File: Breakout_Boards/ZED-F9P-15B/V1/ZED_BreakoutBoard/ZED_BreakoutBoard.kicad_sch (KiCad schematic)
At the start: 15 parts, among them IC1 ZED-F9P-15B, J1 142-0701-801, J2 GPS_Conn_02x04_Top_Bottom

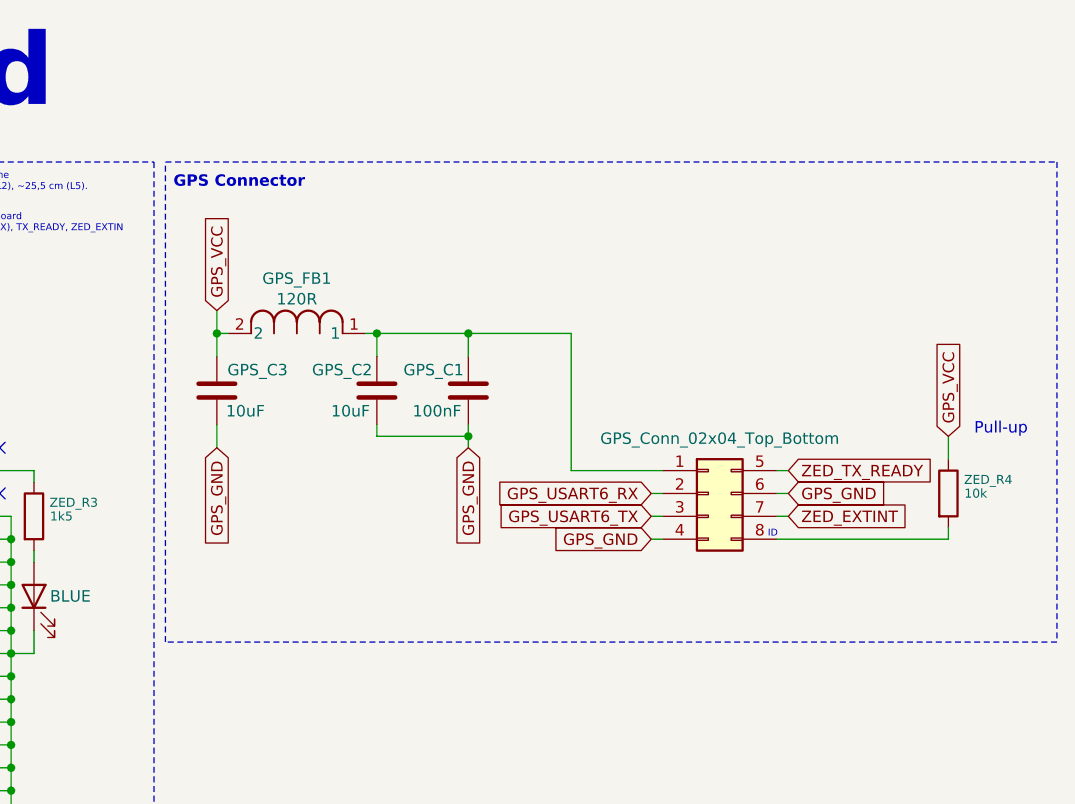
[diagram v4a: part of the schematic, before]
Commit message: fix: swipe filter breakoutboard VCC to main connector side
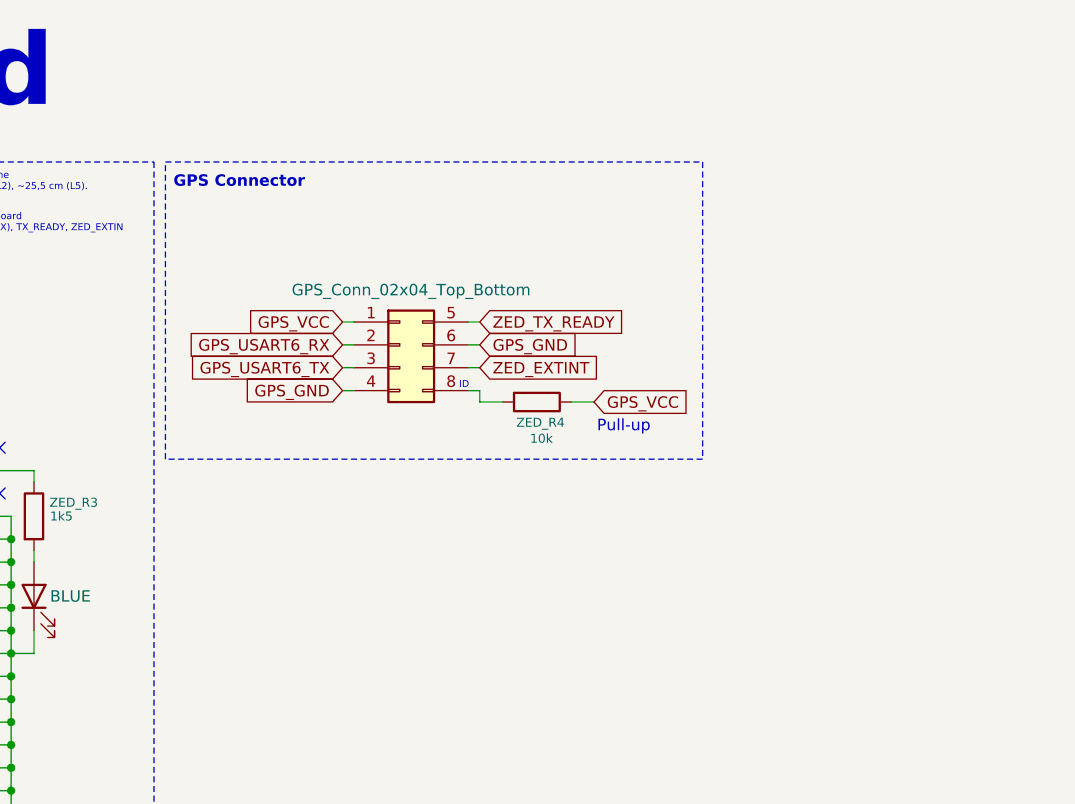
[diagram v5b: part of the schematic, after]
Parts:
- removed GPS_C1: 100nF, Capacitor_SMD:C_0603_1608Metric, symbol Device:C
- removed GPS_C2, GPS_C3: 10uF, Capacitor_SMD:C_0603_1608Metric, symbol Device:C
- removed GPS_FB1: 120R, ZED_Library:IND_25_0805_FRT, symbol ZED_Library:2508051217Y6
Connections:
- net GPS_VCC: now also J2.1 (Pin_1)
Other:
- moved on the sheet: ZED_R4

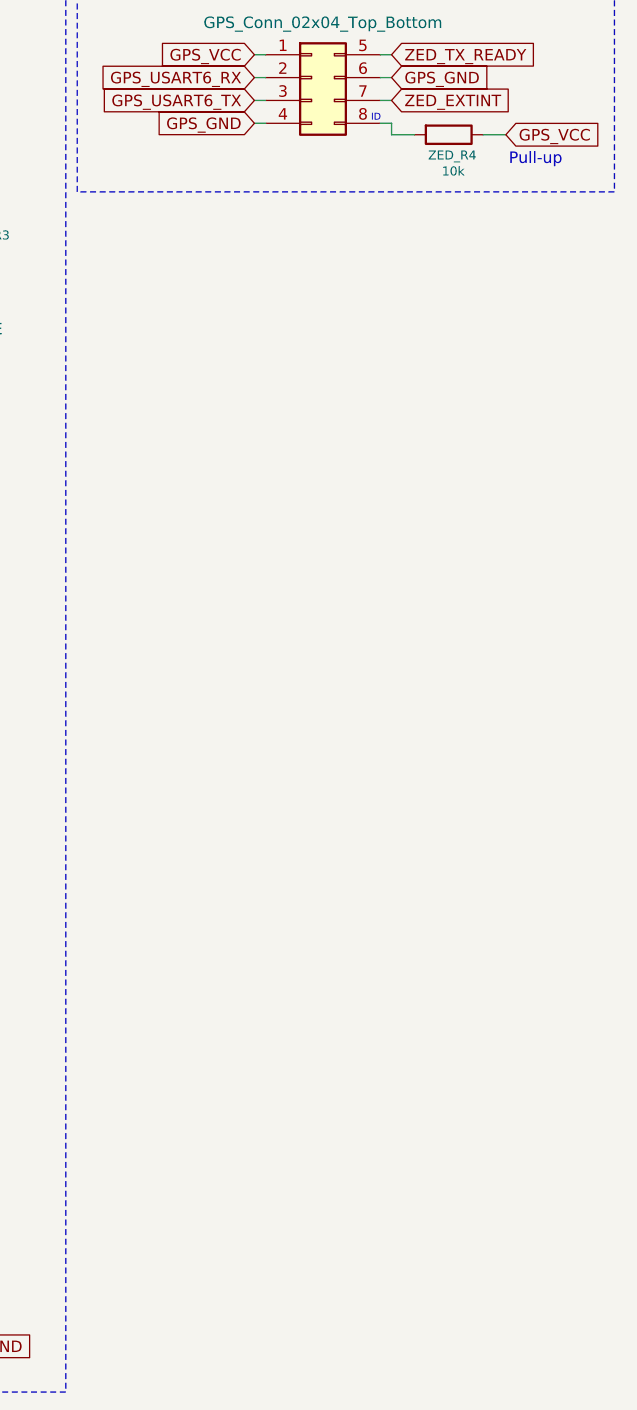
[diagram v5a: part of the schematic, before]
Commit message: feat: add mounting holes M2 & cleanup unnecessary components & add sma footprint
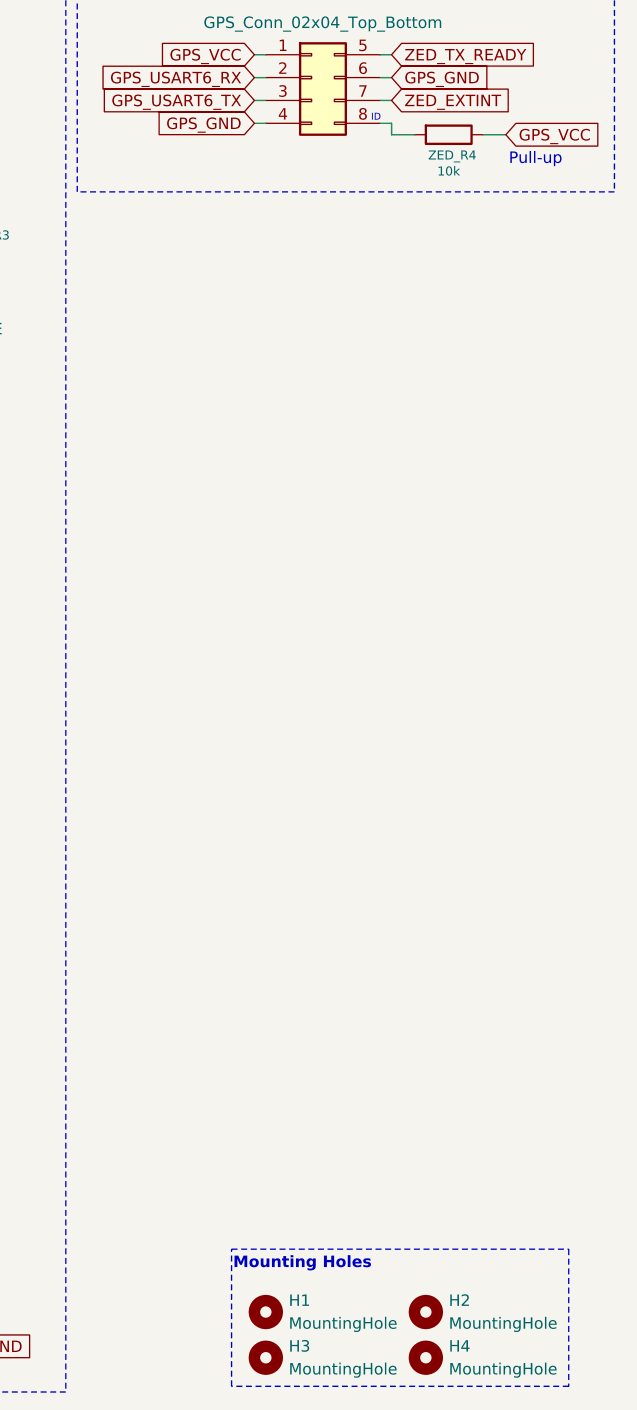
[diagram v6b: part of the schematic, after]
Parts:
- added H1, H2, H3, H4: MountingHole, MountingHole:MountingHole_2.2mm_M2, symbol Mechanical:MountingHole
- J1: footprint CONN_142-0701-801 -> ZED_Library:CONN_142-0701-801
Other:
- note added: "Mounting Holes"

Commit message: WIP : finition layout, fix connecteur GPS, passage 4 couches -> 6 couches
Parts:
- J2: footprint Connector_PinHeader_2.00mm:PinHeader_2x04_P2.00mm_Horizontal -> Connector_PinHeader_2.54mm:PinHeader_2x04_P2.54mm_Vertical
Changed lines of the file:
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@@
 			)
 		)
-		(property "Footprint" "Connector_PinHeader_2.00mm:PinHeader_2x04_P2.00mm_Horizontal"
+		(property "Footprint" "Connector_PinHeader_2.54mm:PinHeader_2x04_P2.54mm_Vertical"
 			(at 147.32 50.8 0)
 			(effects
